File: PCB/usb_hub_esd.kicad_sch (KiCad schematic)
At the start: 3 parts, among them U5 TPAZ1043-04F, U6 TPAZ1043-04F, U7 TPAZ1043-04F

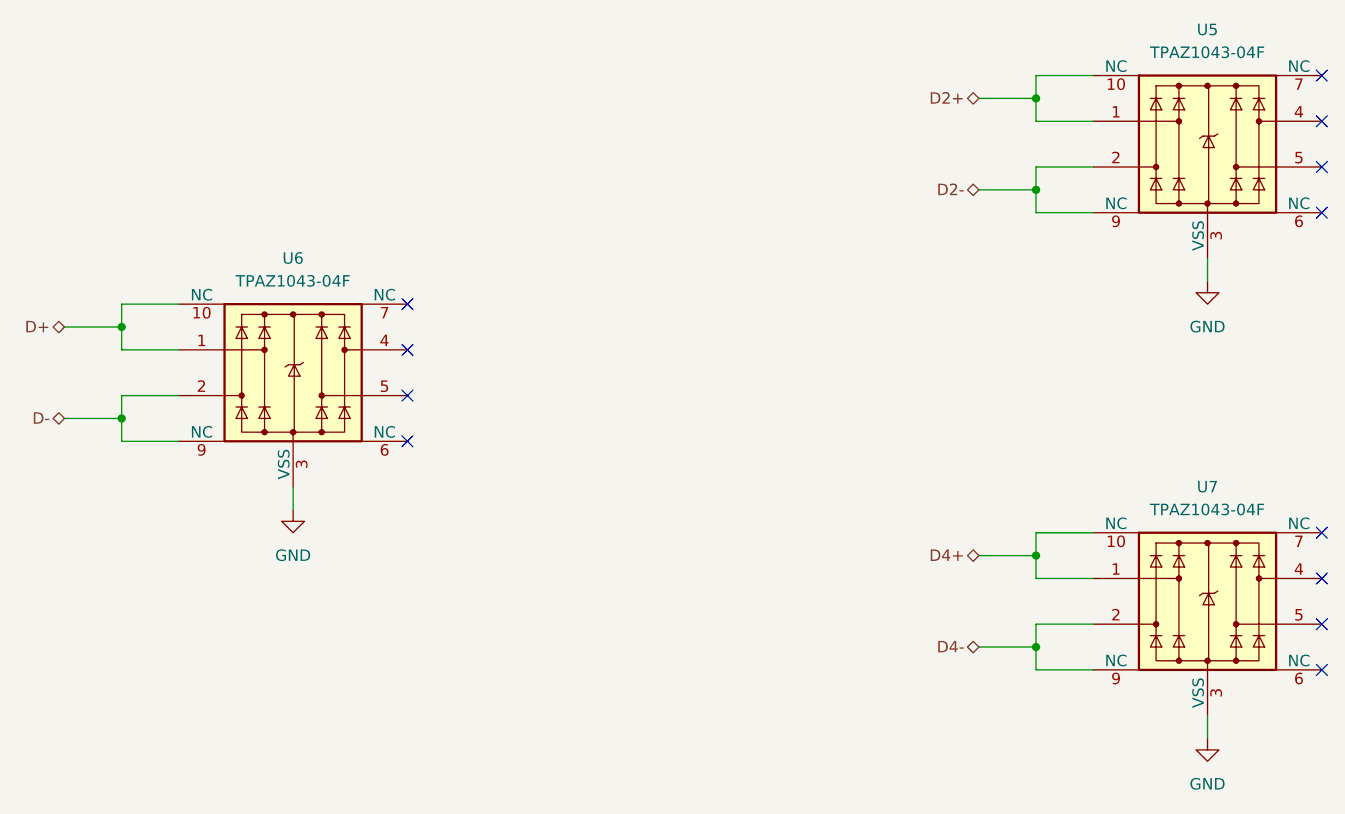
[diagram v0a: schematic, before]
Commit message: Improve the ESD protection
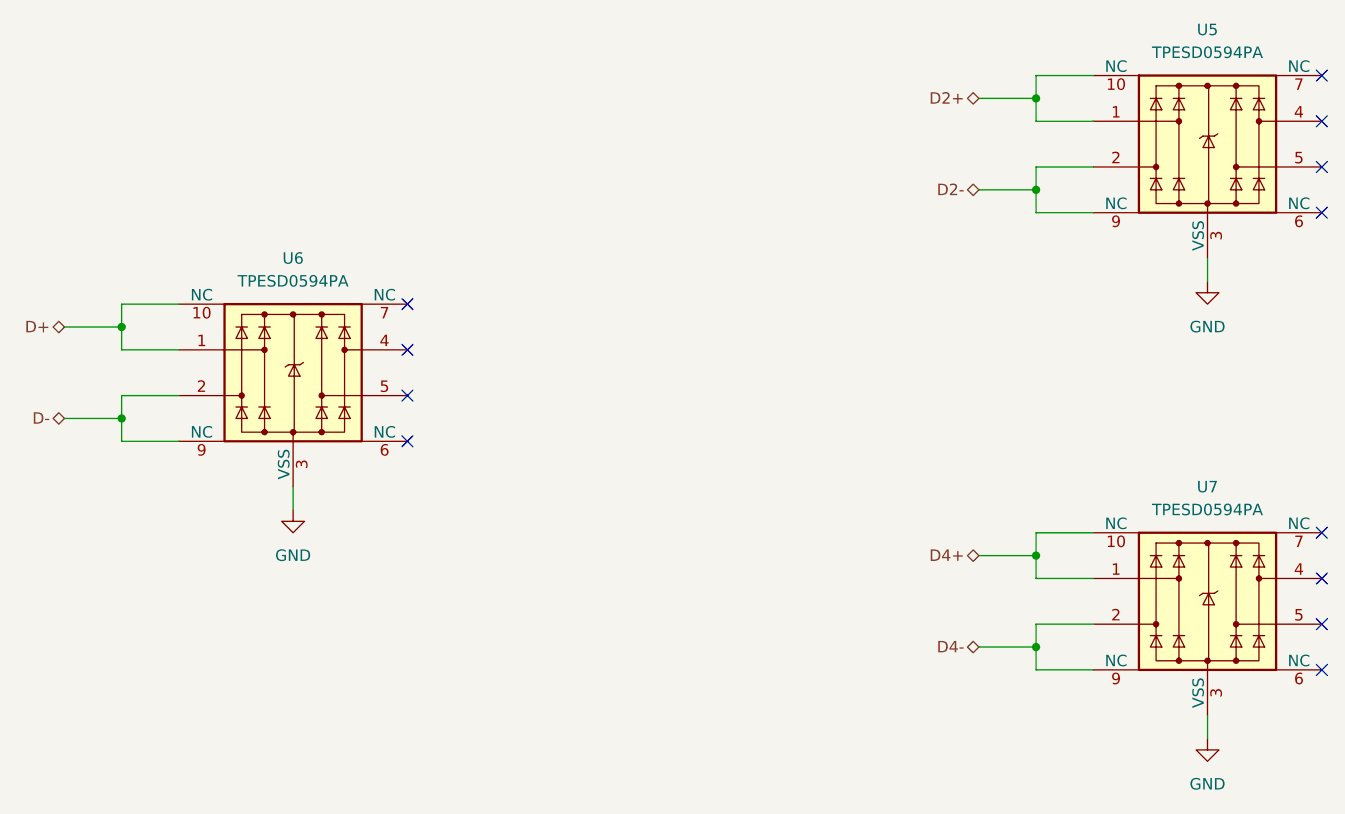
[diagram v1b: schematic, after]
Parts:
- U5, U6, U7: value TPAZ1043-04F -> TPESD0594PA; LCSC C2827673 -> C42436622; Part_number TPAZ1043-04F -> TPESD0594PA
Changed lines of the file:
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@@
 			)
 		)
-		(property "Value" "TPAZ1043-04F"
+		(property "Value" "TPESD0594PA"
 			(at 88.9 72.39 0)
 			(effects
@@
 			)
 		)
-		(property "Datasheet" "https://www.lcsc.com/datasheet/lcsc_datasheet_2411121100_TECH-PUBLIC-TPAZ1043-04F_C2827673.pdf"
+		(property "Datasheet" "https://www.lcsc.com/datasheet/lcsc_datasheet_2501161435_TECH-PUBLIC-TPESD0594PA_C42436622.pdf"
 			(at 88.9 82.55 0)
 			(effects
@@
 			)
 		)
-		(property "LCSC" "C2827673"
+		(property "LCSC" "C42436622"
 			(at 88.9 82.55 0)
 			(effects
@@
 			)
 		)
-		(property "Part_number" "TPAZ1043-04F"
+		(property "Part_number" "TPESD0594PA"
 			(at 88.9 82.55 0)
 			(effects
@@
 		(dnp no)
 		(fields_autoplaced yes)
-		(property "Reference" "#PWR028"
+		(property "Reference" "#PWR030"
 			(at 190.5 78.74 0)
 			(effects
@@
 			(project "clavier"
 				(path "/6362c6e0-59ef-40d3-b6e0-7e9dfe7b9b20/f3d926d4-179d-4033-9062-145e3f3d7f6d/ef8929de-a747-4f3a-ab77-4865a3483dd3"
-					(reference "#PWR028")
+					(reference "#PWR030")
 					(unit 1)
 				)
@@
 			)
 		)
-		(property "Value" "TPAZ1043-04F"
+		(property "Value" "TPESD0594PA"
 			(at 190.5 97.79 0)
 			(effects
@@
 			)
 		)
-		(property "Datasheet" "https://www.lcsc.com/datasheet/lcsc_datasheet_2411121100_TECH-PUBLIC-TPAZ1043-04F_C2827673.pdf"
+		(property "Datasheet" "https://www.lcsc.com/datasheet/lcsc_datasheet_2501161435_TECH-PUBLIC-TPESD0594PA_C42436622.pdf"
 			(at 190.5 107.95 0)
 			(effects
@@
 			)
 		)
-		(property "LCSC" "C2827673"
+		(property "LCSC" "C42436622"
 			(at 190.5 107.95 0)
 			(effects
@@
 			)
 		)
-		(property "Part_number" "TPAZ1043-04F"
+		(property "Part_number" "TPESD0594PA"
 			(at 190.5 107.95 0)
 			(effects
@@
 		(dnp no)
 		(fields_autoplaced yes)
-		(property "Reference" "#PWR030"
+		(property "Reference" "#PWR032"
 			(at 190.5 129.54 0)
 			(effects
@@
 			(project "clavier"
 				(path "/6362c6e0-59ef-40d3-b6e0-7e9dfe7b9b20/f3d926d4-179d-4033-9062-145e3f3d7f6d/ef8929de-a747-4f3a-ab77-4865a3483dd3"
-					(reference "#PWR030")
+					(reference "#PWR032")
 					(unit 1)
 				)
@@
 			)
 		)
-		(property "Value" "TPAZ1043-04F"
+		(property "Value" "TPESD0594PA"
 			(at 190.5 46.99 0)
 			(effects
@@
 			)
 		)
-		(property "Datasheet" "https://www.lcsc.com/datasheet/lcsc_datasheet_2411121100_TECH-PUBLIC-TPAZ1043-04F_C2827673.pdf"
+		(property "Datasheet" "https://www.lcsc.com/datasheet/lcsc_datasheet_2501161435_TECH-PUBLIC-TPESD0594PA_C42436622.pdf"
 			(at 190.5 57.15 0)
 			(effects
@@
 			)
 		)
-		(property "LCSC" "C2827673"
+		(property "LCSC" "C42436622"
 			(at 190.5 57.15 0)
 			(effects
@@
 			)
 		)
-		(property "Part_number" "TPAZ1043-04F"
+		(property "Part_number" "TPESD0594PA"
 			(at 190.5 57.15 0)
 			(effects
@@
 		(dnp no)
 		(fields_autoplaced yes)
-		(property "Reference" "#PWR029"
+		(property "Reference" "#PWR031"
 			(at 88.9 104.14 0)
 			(effects
@@
 			(project "clavier"
 				(path "/6362c6e0-59ef-40d3-b6e0-7e9dfe7b9b20/f3d926d4-179d-4033-9062-145e3f3d7f6d/ef8929de-a747-4f3a-ab77-4865a3483dd3"
-					(reference "#PWR029")
-					(unit 1)
-				)
+					(reference "#PWR031")
+					(unit 1)
+				)

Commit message: Complete the PCB routing
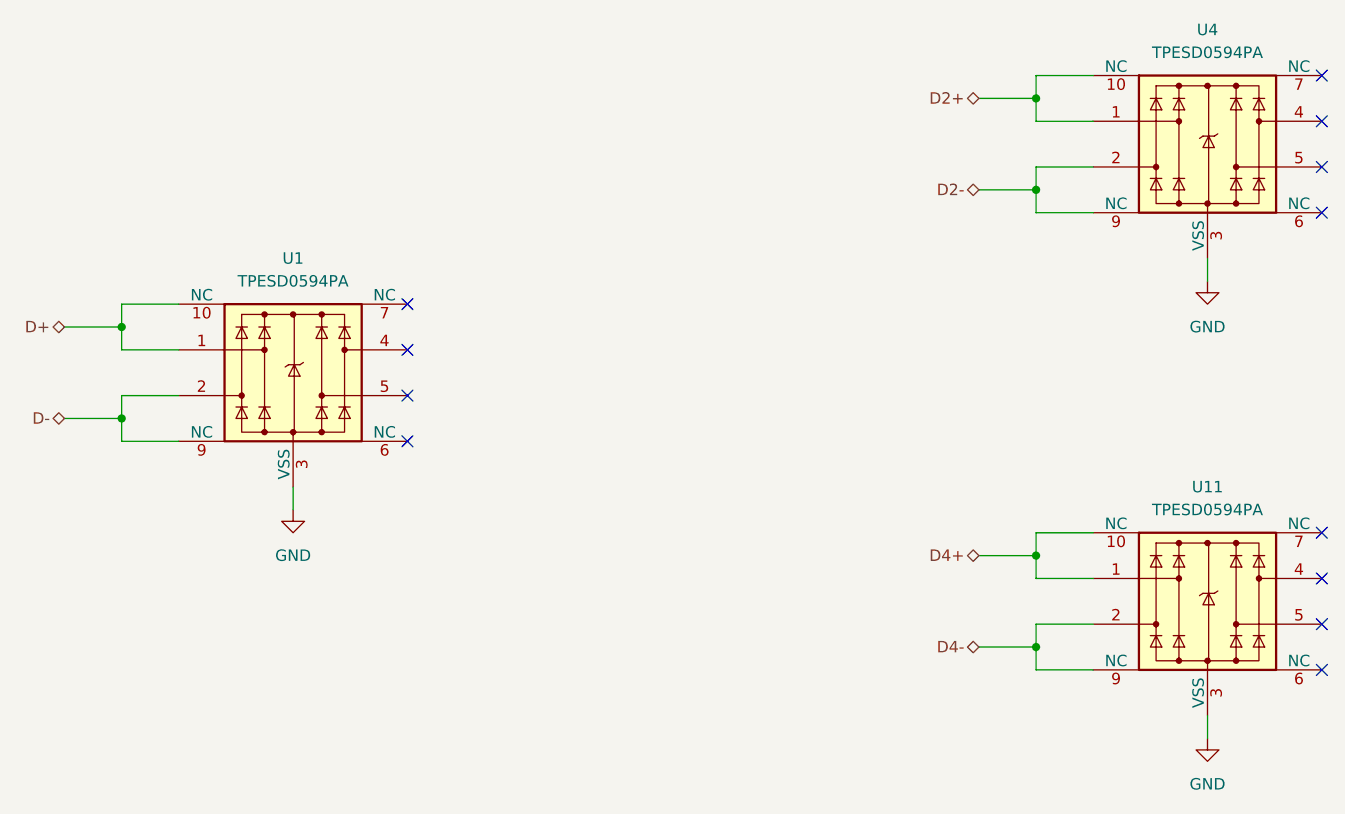
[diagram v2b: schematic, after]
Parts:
- renumbered U6 to U1, U7 to U11, U5 to U4
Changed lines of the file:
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@@
 	(title_block
 		(title "Clavier - USB hub ESD protection")
-		(date "2025-06-21")
+		(date "2025-06-22")
 		(rev "1.0")
 		(company "Copyright (c) 2025 L. Sartory")
@@
 		(dnp no)
 		(fields_autoplaced yes)
-		(property "Reference" "U6"
+		(property "Reference" "U1"
 			(at 88.9 69.85 0)
 			(effects
@@
 			(project "clavier"
 				(path "/6362c6e0-59ef-40d3-b6e0-7e9dfe7b9b20/f3d926d4-179d-4033-9062-145e3f3d7f6d/ef8929de-a747-4f3a-ab77-4865a3483dd3"
-					(reference "U6")
+					(reference "U1")
 					(unit 1)
 				)
@@
 		(dnp no)
 		(fields_autoplaced yes)
-		(property "Reference" "U7"
+		(property "Reference" "U11"
 			(at 190.5 95.25 0)
 			(effects
@@
 			(project "clavier"
 				(path "/6362c6e0-59ef-40d3-b6e0-7e9dfe7b9b20/f3d926d4-179d-4033-9062-145e3f3d7f6d/ef8929de-a747-4f3a-ab77-4865a3483dd3"
-					(reference "U7")
+					(reference "U11")
 					(unit 1)
 				)
@@
 		(dnp no)
 		(fields_autoplaced yes)
-		(property "Reference" "U5"
+		(property "Reference" "U4"
 			(at 190.5 44.45 0)
 			(effects
@@
 			(project "clavier"
 				(path "/6362c6e0-59ef-40d3-b6e0-7e9dfe7b9b20/f3d926d4-179d-4033-9062-145e3f3d7f6d/ef8929de-a747-4f3a-ab77-4865a3483dd3"
-					(reference "U5")
+					(reference "U4")
 					(unit 1)
 				)
